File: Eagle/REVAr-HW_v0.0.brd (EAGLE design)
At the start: 101.6 x 53.3 mm, 74 parts, among them IC1 MC33269ST-5.0T3, IC2 MC33269D-5.0, IC3 ATMEGA2560-16AU, IC4 ATMEGA8U2-MU, IC5 LM358D, IC6 LP2985-33DBVR, Q1 16MHz, Q2 16MHz, T2 FDN340P, X1 DC21MMX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

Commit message: [HW] Add SPEC gas sensors and communication via RS485 with Arduino
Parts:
- added U$10, U$12, U$18, U$20, U$7, U$8: RS485-TTL-CONVERTER, diy-modules:RS485-TTL-CONVERTER
- added U$11, U$13, U$14, U$15, U$16, U$17, U$19, U$9: (no value), spec-sensors:DGS-XX
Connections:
- new net A-485: U$10.J2.3, U$12.J2.3, U$18.J2.3, U$20.J2.3, U$7.J2.3, U$8.J2.3
- new net B-485: U$10.J2.2, U$12.J2.2, U$18.J2.2, U$20.J2.2, U$7.J2.2, U$8.J2.2
- new net N$1: U$16.P$3, U$7.J1.4
- new net N$10: U$12.J1.1, U$17.P$2
- new net N$11: U$18.J1.4, U$19.P$3
- new net N$12: U$18.J1.1, U$19.P$2
- new net N$4: U$16.P$2, U$7.J1.1
- new net N$5: U$10.J1.4, U$11.P$3
- new net N$6: U$10.J1.1, U$11.P$2
- new net N$7: U$8.J1.4, U$9.P$3
- new net N$8: U$8.J1.1, U$9.P$2
- new net N$9: U$12.J1.4, U$17.P$3
- net GND: now also U$10.J2.4, U$11.P$6, U$12.J2.4, U$16.P$6, U$17.P$6, U$18.J2.4, U$19.P$6, U$20.J2.4, U$7.J2.4, U$8.J2.4, U$9.P$6
- net PA0: no longer U$1.J2.5
- net PA1: no longer U$1.J2.6
- net PE3: now also U$10.J1.2, U$10.J1.3
- net PE4: now also U$1.J2.5
- net PE5: now also U$1.J2.6
- net PG5: now also U$7.J1.2, U$7.J1.3
- net PH3: now also U$8.J1.2, U$8.J1.3
- net PH4: now also U$12.J1.2, U$12.J1.3
- net PH5: now also U$18.J1.2, U$18.J1.3
- net PH6: now also U$20.J1.2, U$20.J1.3
- net VCC: now also U$10.J2.1, U$11.P$8, U$12.J2.1, U$16.P$8, U$17.P$8, U$18.J2.1, U$19.P$8, U$20.J2.1, U$7.J2.1, U$8.J2.1, U$9.P$8

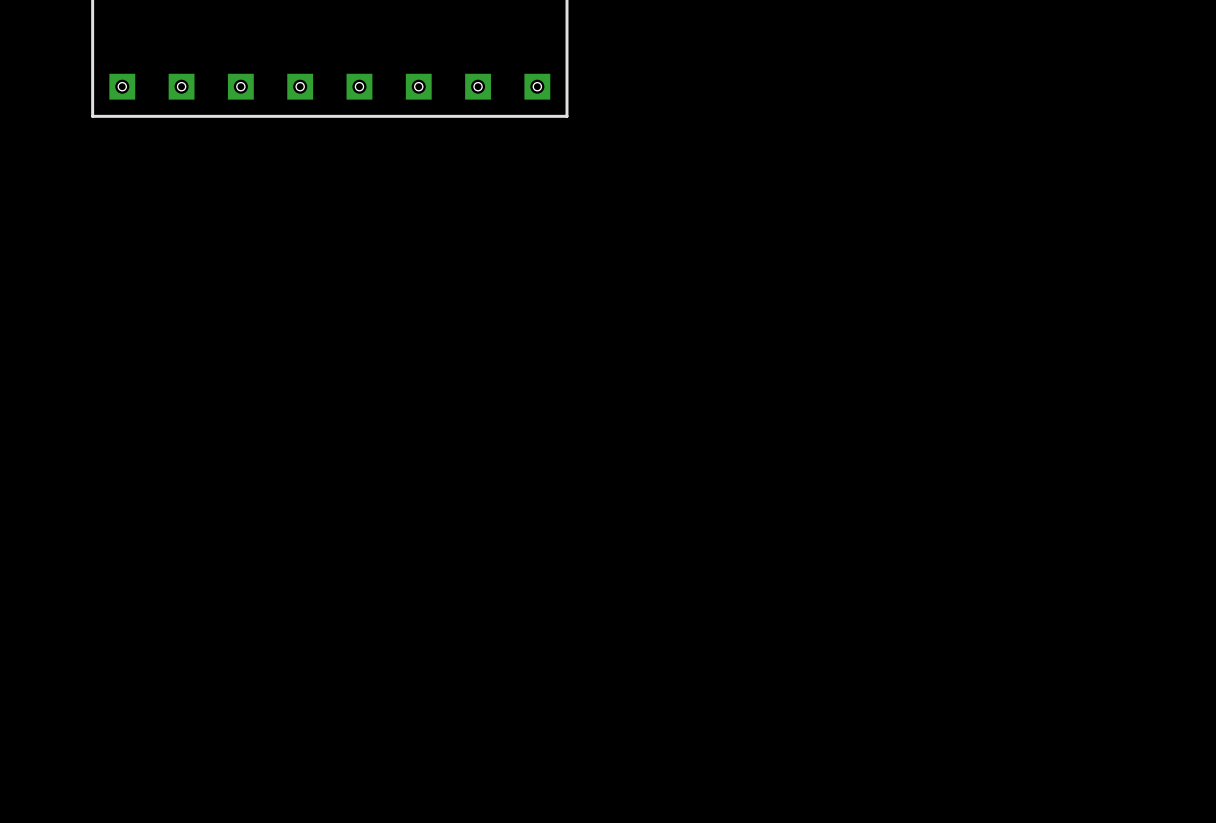
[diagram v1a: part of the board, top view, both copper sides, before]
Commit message: [HW] Add PM UART sensor SDS011 to design
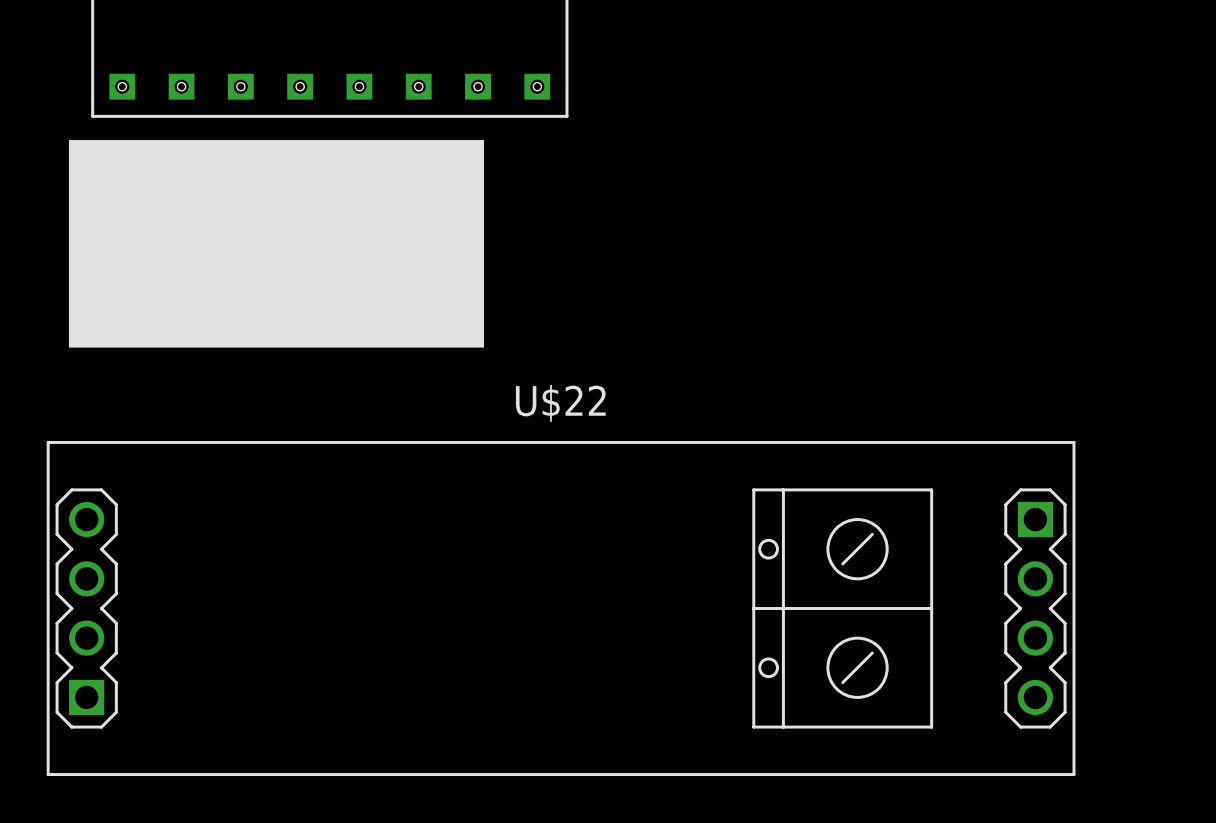
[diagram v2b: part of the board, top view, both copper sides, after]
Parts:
- added U$21: SDS011, gas-sensors:SDS011
- added U$22: RS485-TTL-CONVERTER, diy-modules:RS485-TTL-CONVERTER
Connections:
- new net N$13: U$21.P$6, U$22.J1.4
- new net N$14: U$21.P$7, U$22.J1.1
- net A-485: now also U$22.J2.3
- net B-485: now also U$22.J2.2
- net GND: now also U$21.P$5, U$22.J2.4
- net N$1: now also U$16.P$2; no longer U$16.P$3
- net N$10: now also U$12.J1.4; no longer U$12.J1.1
- net N$11: now also U$8.J1.4, U$9.P$2; no longer U$18.J1.4, U$19.P$3
- net N$12: now also U$12.J1.1, U$17.P$3; no longer U$18.J1.1, U$19.P$2
- net N$4: now also U$16.P$3; no longer U$16.P$2
- net N$5: now also U$11.P$2; no longer U$11.P$3
- net N$6: now also U$11.P$3; no longer U$11.P$2
- net N$7: now also U$18.J1.4, U$19.P$2; no longer U$8.J1.4, U$9.P$3
- net N$8: now also U$9.P$3; no longer U$9.P$2
- net N$9: now also U$18.J1.1, U$19.P$3; no longer U$12.J1.4, U$17.P$3
- net PB4: now also U$22.J1.2, U$22.J1.3
- net RXD2: now also U$20.J1.4
- net TXD2: now also U$20.J1.1
- net VCC: now also U$21.P$3, U$22.J2.1
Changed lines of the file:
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@@
 <element name="U$19" library="spec-sensors" package="DGS-XX" value="" x="-95.631" y="-354.711"/>
 <element name="U$20" library="diy-modules" package="RS485-TTL-CONVERTER" value="RS485-TTL-CONVERTER" x="-74.549" y="-334.518"/>
+<element name="U$21" library="gas-sensors" package="SDS011" value="SDS011" x="-96.647" y="-364.617"/>
+<element name="U$22" library="diy-modules" package="RS485-TTL-CONVERTER" value="RS485-TTL-CONVERTER" x="-75.565" y="-375.793"/>
 </elements>
 <signals>
@@
 <contactref element="U$20" pad="J2.4"/>
 <contactref element="U$19" pad="P$6"/>
+<contactref element="U$22" pad="J2.4"/>
+<contactref element="U$21" pad="P$5"/>
+<wire x1="-81.661" y1="-353.441" x2="-85.217" y2="-363.347" width="0" layer="19" extent="1-1"/>
 <wire x1="-54.229" y1="-338.328" x2="-81.661" y2="-353.441" width="0" layer="19" extent="1-1"/>
 <wire x1="-54.229" y1="-318.262" x2="-54.229" y2="-338.328" width="0" layer="19" extent="1-1"/>
@@
 <wire x1="-54.229" y1="-235.458" x2="-54.229" y2="-266.827" width="0" layer="19" extent="1-1"/>
 <wire x1="-81.661" y1="-250.571" x2="-54.229" y2="-235.458" width="0" layer="19" extent="1-1"/>
+<wire x1="-55.245" y1="-379.603" x2="-85.217" y2="-363.347" width="0" layer="19" extent="1-1"/>
 <wire x1="-78.994" y1="-185.293" x2="-54.229" y2="-235.458" width="0" layer="19" extent="1-1"/>
 <wire x1="13.589" y1="-69.85" x2="-78.994" y2="-185.293" width="0" layer="19" extent="1-1"/>
@@
 <wire x1="42.9044" y1="23.3464" x2="42.8" y2="23.3464" width="0.2032" layer="1"/>
 <wire x1="36.322" y1="23.368" x2="42.926" y2="23.368" width="0.2032" layer="1"/>
+<contactref element="U$22" pad="J1.3"/>
+<contactref element="U$22" pad="J1.2"/>
+<wire x1="-95.885" y1="-374.523" x2="-95.885" y2="-377.063" width="0" layer="19" extent="1-1"/>
+<wire x1="36.322" y1="23.368" x2="-95.885" y2="-374.523" width="0" layer="19" extent="1-1"/>
 </signal>
 <signal name="PE5">
@@
 <wire x1="41.021" y1="30.099" x2="42.672" y2="31.75" width="0.2032" layer="16"/>
 <via x="41.021" y="28.829" extent="1-16" drill="0.4064" shape="octagon"/>
+<contactref element="U$20" pad="J1.4"/>
+<wire x1="41.0384" y1="28.8464" x2="-94.869" y2="-330.708" width="0" layer="19" extent="1-1"/>
 </signal>
 <signal name="RXD3">
@@
 <wire x1="39.751" y1="29.591" x2="42.164" y2="32.004" width="0.2032" layer="16"/>
 <via x="39.751" y="28.829" extent="1-16" drill="0.4064" shape="octagon"/>
+<contactref element="U$20" pad="J1.1"/>
+<wire x1="39.878" y1="27.94" x2="-94.869" y2="-338.328" width="0" layer="19" extent="1-1"/>
 </signal>
 <signal name="TXD3">
@@
 <contactref element="U$20" pad="J2.1"/>
 <contactref element="U$19" pad="P$8"/>
+<contactref element="U$22" pad="J2.1"/>
+<contactref element="U$21" pad="P$3"/>
+<wire x1="-76.581" y1="-353.441" x2="-90.297" y2="-363.347" width="0" layer="19" extent="1-1"/>
+<wire x1="-55.245" y1="-371.983" x2="-76.581" y2="-353.441" width="0" layer="19" extent="1-1"/>
 <wire x1="-54.229" y1="-330.708" x2="-76.581" y2="-353.441" width="0" layer="19" extent="1-1"/>
 <wire x1="-54.229" y1="-310.642" x2="-54.229" y2="-330.708" width="0" layer="19" extent="1-1"/>
@@
 <wire x1="-11.176" y1="-47.244" x2="-24.384" y2="-51.689" width="0" layer="19" extent="1-1"/>
 </signal>
-<signal name="N$1">
-<contactref element="U$16" pad="P$3"/>
-<contactref element="U$7" pad="J1.4"/>
-<wire x1="-86.614" y1="-185.293" x2="-27.051" y2="-62.23" width="0" layer="19" extent="1-1"/>
-</signal>
-<signal name="N$4">
-<contactref element="U$16" pad="P$2"/>
-<contactref element="U$7" pad="J1.1"/>
-<wire x1="-89.154" y1="-185.293" x2="-27.051" y2="-69.85" width="0" layer="19" extent="1-1"/>
-</signal>
 <signal name="B-485">
 <contactref element="U$7" pad="J2.2"/>
@@
 <contactref element="U$18" pad="J2.2"/>
 <contactref element="U$20" pad="J2.2"/>
+<contactref element="U$22" pad="J2.2"/>
+<wire x1="-54.229" y1="-333.248" x2="-55.245" y2="-374.523" width="0" layer="19" extent="1-1"/>
 <wire x1="-54.229" y1="-313.182" x2="-54.229" y2="-333.248" width="0" layer="19" extent="1-1"/>
 <wire x1="-54.229" y1="-281.813" x2="-54.229" y2="-313.182" width="0" layer="19" extent="1-1"/>
@@
 <contactref element="U$18" pad="J2.3"/>
 <contactref element="U$20" pad="J2.3"/>
+<contactref element="U$22" pad="J2.3"/>
+<wire x1="-54.229" y1="-335.788" x2="-55.245" y2="-377.063" width="0" layer="19" extent="1-1"/>
 <wire x1="-54.229" y1="-315.722" x2="-54.229" y2="-335.788" width="0" layer="19" extent="1-1"/>
 <wire x1="-54.229" y1="-284.353" x2="-54.229" y2="-315.722" width="0" layer="19" extent="1-1"/>
@@
 <wire x1="13.589" y1="-67.31" x2="-54.229" y2="-232.918" width="0" layer="19" extent="1-1"/>
 </signal>
+<signal name="N$1">
+<contactref element="U$16" pad="P$2"/>
+<contactref element="U$7" pad="J1.4"/>
+<wire x1="-89.154" y1="-185.293" x2="-27.051" y2="-62.23" width="0" layer="19" extent="1-1"/>
+</signal>
+<signal name="N$4">
+<contactref element="U$16" pad="P$3"/>
+<contactref element="U$7" pad="J1.1"/>
+<wire x1="-86.614" y1="-185.293" x2="-27.051" y2="-69.85" width="0" layer="19" extent="1-1"/>
+</signal>
 <signal name="N$5">
+<contactref element="U$11" pad="P$2"/>
+<contactref element="U$10" pad="J1.4"/>
+<wire x1="-94.869" y1="-227.838" x2="-91.821" y2="-250.571" width="0" layer="19" extent="1-1"/>
+</signal>
+<signal name="N$6">
 <contactref element="U$11" pad="P$3"/>
-<contactref element="U$10" pad="J1.4"/>
-<wire x1="-94.869" y1="-227.838" x2="-89.281" y2="-250.571" width="0" layer="19" extent="1-1"/>
-</signal>
-<signal name="N$6">
-<contactref element="U$11" pad="P$2"/>
 <contactref element="U$10" pad="J1.1"/>
-<wire x1="-94.869" y1="-235.458" x2="-91.821" y2="-250.571" width="0" layer="19" extent="1-1"/>
+<wire x1="-94.869" y1="-235.458" x2="-89.281" y2="-250.571" width="0" layer="19" extent="1-1"/>
 </signal>
 <signal name="N$7">
+<contactref element="U$19" pad="P$2"/>
+<contactref element="U$18" pad="J1.4"/>
+<wire x1="-94.869" y1="-310.642" x2="-91.821" y2="-353.441" width="0" layer="19" extent="1-1"/>
+</signal>
+<signal name="N$9">
+<contactref element="U$19" pad="P$3"/>
+<contactref element="U$18" pad="J1.1"/>
+<wire x1="-94.869" y1="-318.262" x2="-89.281" y2="-353.441" width="0" layer="19" extent="1-1"/>
+</signal>
+<signal name="N$11">
+<contactref element="U$9" pad="P$2"/>
+<contactref element="U$8" pad="J1.4"/>
+<wire x1="-94.869" y1="-259.207" x2="-91.821" y2="-302.006" width="0" layer="19" extent="1-1"/>
+</signal>
+<signal name="N$8">
 <contactref element="U$9" pad="P$3"/>
-<contactref element="U$8" pad="J1.4"/>
-<wire x1="-94.869" y1="-259.207" x2="-89.281" y2="-302.006" width="0" layer="19" extent="1-1"/>
-</signal>
-<signal name="N$8">
-<contactref element="U$9" pad="P$2"/>
 <contactref element="U$8" pad="J1.1"/>
-<wire x1="-94.869" y1="-266.827" x2="-91.821" y2="-302.006" width="0" layer="19" extent="1-1"/>
-</signal>
-<signal name="N$9">
-<contactref element="U$17" pad="P$3"/>
-<contactref element="U$12" pad="J1.4"/>
-<wire x1="-67.818" y1="-302.006" x2="-94.869" y2="-279.273" width="0" layer="19" extent="1-1"/>
+<wire x1="-94.869" y1="-266.827" x2="-89.281" y2="-302.006" width="0" layer="19" extent="1-1"/>
 </signal>
 <signal name="N$10">
 <contactref element="U$17" pad="P$2"/>
+<contactref element="U$12" pad="J1.4"/>
+<wire x1="-70.358" y1="-302.006" x2="-94.869" y2="-279.273" width="0" layer="19" extent="1-1"/>
+</signal>
+<signal name="N$12">
+<contactref element="U$17" pad="P$3"/>
 <contactref element="U$12" pad="J1.1"/>
-<wire x1="-70.358" y1="-302.006" x2="-94.869" y2="-286.893" width="0" layer="19" extent="1-1"/>
-</signal>
-<signal name="N$11">
-<contactref element="U$19" pad="P$3"/>
-<contactref element="U$18" pad="J1.4"/>
-<wire x1="-94.869" y1="-310.642" x2="-89.281" y2="-353.441" width="0" layer="19" extent="1-1"/>
-</signal>
-<signal name="N$12">
-<contactref element="U$19" pad="P$2"/>
-<contactref element="U$18" pad="J1.1"/>
-<wire x1="-94.869" y1="-318.262" x2="-91.821" y2="-353.441" width="0" layer="19" extent="1-1"/>
+<wire x1="-67.818" y1="-302.006" x2="-94.869" y2="-286.893" width="0" layer="19" extent="1-1"/>
+</signal>
+<signal name="N$13">
+<contactref element="U$21" pad="P$6"/>
+<contactref element="U$22" pad="J1.4"/>
+<wire x1="-82.677" y1="-363.347" x2="-95.885" y2="-371.983" width="0" layer="19" extent="1-1"/>
+</signal>
+<signal name="N$14">
+<contactref element="U$21" pad="P$7"/>
+<contactref element="U$22" pad="J1.1"/>
+<wire x1="-80.137" y1="-363.347" x2="-95.885" y2="-379.603" width="0" layer="19" extent="1-1"/>
 </signal>
 </signals>

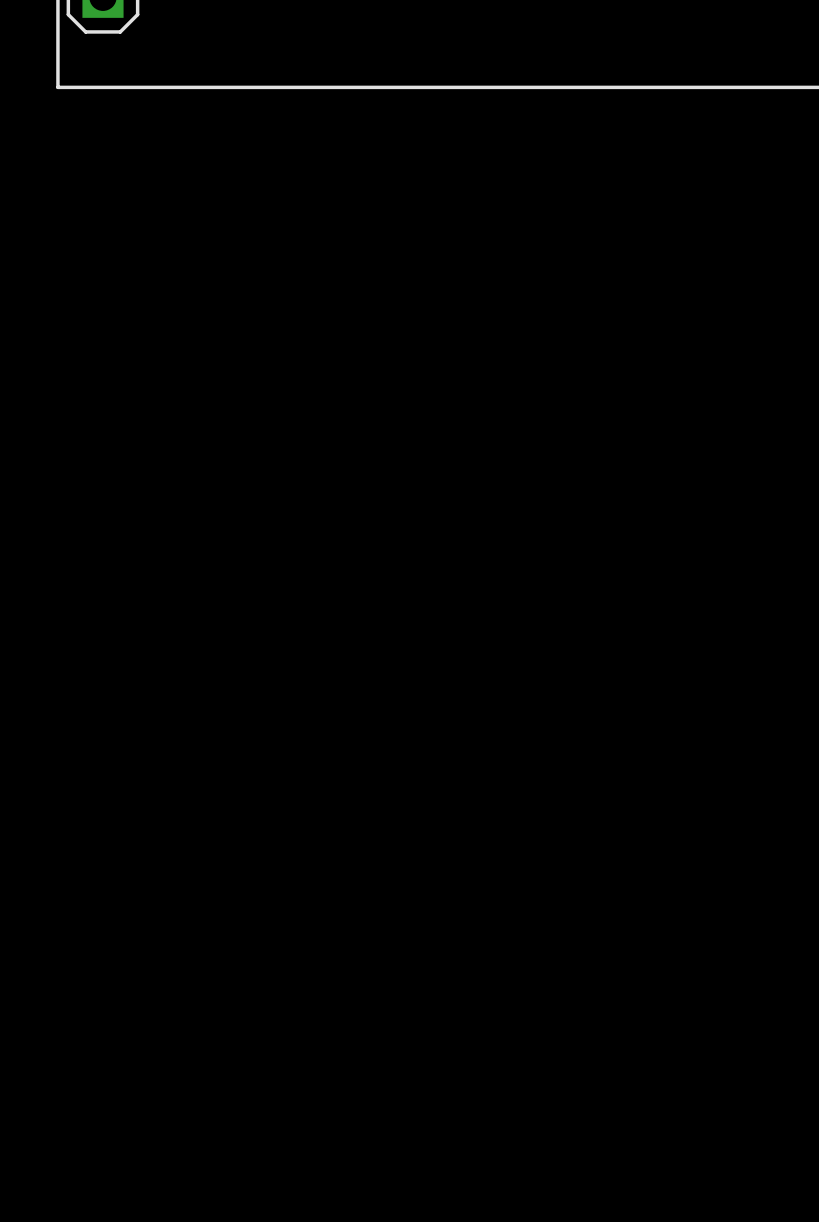
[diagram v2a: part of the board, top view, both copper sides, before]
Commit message: [HW] Add PCF8574 I2C port expander for LCD Display
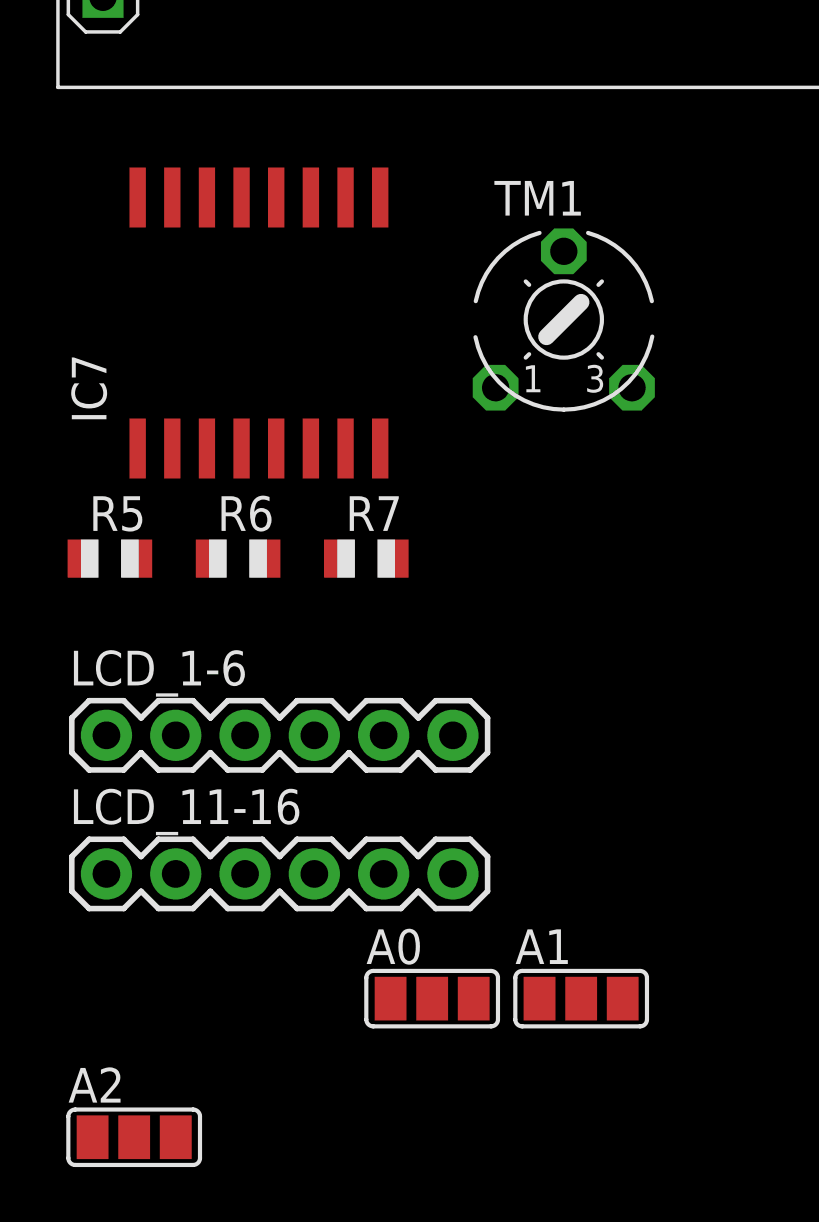
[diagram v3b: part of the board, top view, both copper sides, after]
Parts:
- added A0, A1, A2: (no value), SparkFun:SJ_2
- added IC7: PCF8574T, micro-philips:SO16W
- added LCD_1-6, LCD_11-16: (no value), SparkFun-Connectors:1X06
- added R5: 100, adafruit:R0805
- added R6, R7: 10k, adafruit:R0805
- added TM1: 1K, adafruit:6MM
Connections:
- new net A0: A0.2, IC7.1
- new net A1: A1.2, IC7.2
- new net A2: A2.2, IC7.3
- new net ANODE: LCD_11-16.5, R5.2
- new net CONTR: LCD_1-6.3, TM1.S
- new net DB4: IC7.4, LCD_11-16.1
- new net DB5: IC7.5, LCD_11-16.2
- new net DB6: IC7.6, LCD_11-16.3
- new net DB7: IC7.7, LCD_11-16.4
- new net ENABLE: IC7.11, LCD_1-6.6
- new net RS: IC7.9, LCD_1-6.4
- new net RW: IC7.10, LCD_1-6.5
- net GND: now also A0.1, A1.1, A2.1, IC7.8, LCD_1-6.1, LCD_11-16.6, TM1.E
- net SCL: now also IC7.14, R7.1
- net SDA: now also IC7.15, R6.1
- net VCC: now also A0.3, A1.3, A2.3, IC7.16, LCD_1-6.2, R5.1, R6.2, R7.2, TM1.A
